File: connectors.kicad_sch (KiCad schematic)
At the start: 4 parts, among them J1 Conn_02x03_Odd_Even, J2 Conn_01x04_Pin, J3 Conn_01x09_Pin, J4 Conn_01x04_Pin

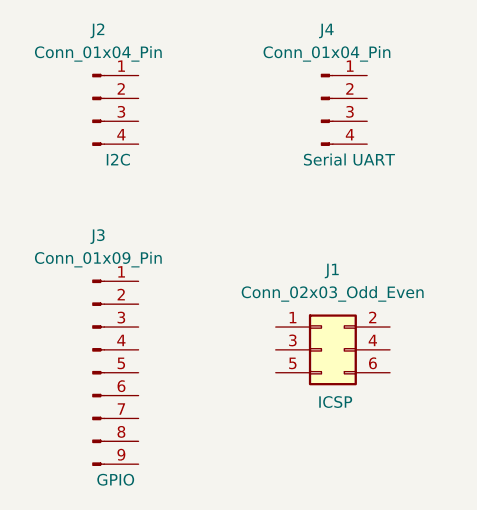
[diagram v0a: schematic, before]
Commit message: completed symbol-footprint association.
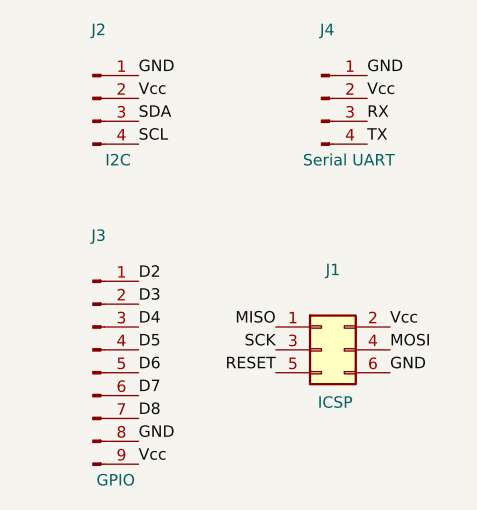
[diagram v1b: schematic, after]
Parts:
- J1: footprint (none) -> Connector_PinHeader_2.54mm:PinHeader_2x03_P2.54mm_Vertical
- J2, J4: footprint (none) -> Connector_PinHeader_2.54mm:PinHeader_1x04_P2.54mm_Vertical
- J3: footprint (none) -> Connector_PinHeader_2.54mm:PinHeader_1x09_P2.54mm_Vertical
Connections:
- net D2: now reaches J3.1 (Pin_1)
- net D3: now reaches J3.2 (Pin_2)
- net D4: now reaches J3.3 (Pin_3)
- net D5: now reaches J3.4 (Pin_4)
- net D6: now reaches J3.5 (Pin_5)
- net D7: now reaches J3.6 (Pin_6)
- net D8: now reaches J3.7 (Pin_7)
- net GND: now reaches J3.8 (Pin_8)
- net GND: now also J1.6 (Pin_6), J2.1 (Pin_1), J4.1 (Pin_1)
- net Vcc: now reaches J3.9 (Pin_9)
- net Vcc: now also J1.2 (Pin_2), J2.2 (Pin_2), J4.2 (Pin_2)
- net SDA: now reaches J2.3 (Pin_3)
- net SCL: now reaches J2.4 (Pin_4)
- net MISO: now reaches J1.1 (Pin_1)
- net SCK: now reaches J1.3 (Pin_3)
- net MOSI: now reaches J1.4 (Pin_4)
- net RESET: now reaches J1.5 (Pin_5)
- net RX: now reaches J4.3 (Pin_3)
- net TX: now reaches J4.4 (Pin_4)
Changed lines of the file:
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@@
 	(generator_version "9.0")
 	(paper "A4")
+	(label "GND"
+		(at 144.78 116.84 0)
+		(effects
+			(font
+				(size 1.27 1.27)
+			)
+			(justify left bottom)
+		)
+	)
+	(label "MISO"
+		(at 132.08 111.76 180)
+		(effects
+			(font
+				(size 1.27 1.27)
+			)
+			(justify right bottom)
+		)
+	)
+	(label "D8"
+		(at 116.84 121.92 0)
+		(effects
+			(font
+				(size 1.27 1.27)
+			)
+			(justify left bottom)
+		)
+	)
+	(label "MOSI"
+		(at 144.78 114.3 0)
+		(effects
+			(font
+				(size 1.27 1.27)
+			)
+			(justify left bottom)
+		)
+	)
+	(label "Vcc"
+		(at 144.78 111.76 0)
+		(effects
+			(font
+				(size 1.27 1.27)
+			)
+			(justify left bottom)
+		)
+	)
+	(label "D5"
+		(at 116.84 114.3 0)
+		(effects
+			(font
+				(size 1.27 1.27)
+			)
+			(justify left bottom)
+		)
+	)
+	(label "SDA"
+		(at 116.84 88.9 0)
+		(effects
+			(font
+				(size 1.27 1.27)
+			)
+			(justify left bottom)
+		)
+	)
+	(label "RX"
+		(at 142.24 88.9 0)
+		(effects
+			(font
+				(size 1.27 1.27)
+			)
+			(justify left bottom)
+		)
+	)
+	(label "TX"
+		(at 142.24 91.44 0)
+		(effects
+			(font
+				(size 1.27 1.27)
+			)
+			(justify left bottom)
+		)
+	)
+	(label "D7"
+		(at 116.84 119.38 0)
+		(effects
+			(font
+				(size 1.27 1.27)
+			)
+			(justify left bottom)
+		)
+	)
+	(label "SCK"
+		(at 132.08 114.3 180)
+		(effects
+			(font
+				(size 1.27 1.27)
+			)
+			(justify right bottom)
+		)
+	)
+	(label "D3"
+		(at 116.84 109.22 0)
+		(effects
+			(font
+				(size 1.27 1.27)
+			)
+			(justify left bottom)
+		)
+	)
+	(label "Vcc"
+		(at 116.84 127 0)
+		(effects
+			(font
+				(size 1.27 1.27)
+			)
+			(justify left bottom)
+		)
+	)
+	(label "GND"
+		(at 116.84 124.46 0)
+		(effects
+			(font
+				(size 1.27 1.27)
+			)
+			(justify left bottom)
+		)
+	)
+	(label "Vcc"
+		(at 116.84 86.36 0)
+		(effects
+			(font
+				(size 1.27 1.27)
+			)
+			(justify left bottom)
+		)
+	)
+	(label "GND"
+		(at 116.84 83.82 0)
+		(effects
+			(font
+				(size 1.27 1.27)
+			)
+			(justify left bottom)
+		)
+	)
+	(label "D2"
+		(at 116.84 106.68 0)
+		(effects
+			(font
+				(size 1.27 1.27)
+			)
+			(justify left bottom)
+		)
+	)
+	(label "GND"
+		(at 142.24 83.82 0)
+		(effects
+			(font
+				(size 1.27 1.27)
+			)
+			(justify left bottom)
+		)
+	)
+	(label "D4"
+		(at 116.84 111.76 0)
+		(effects
+			(font
+				(size 1.27 1.27)
+			)
+			(justify left bottom)
+		)
+	)
+	(label "SCL"
+		(at 116.84 91.44 0)
+		(effects
+			(font
+				(size 1.27 1.27)
+			)
+			(justify left bottom)
+		)
+	)
+	(label "Vcc"
+		(at 142.24 86.36 0)
+		(effects
+			(font
+				(size 1.27 1.27)
+			)
+			(justify left bottom)
+		)
+	)
+	(label "D6"
+		(at 116.84 116.84 0)
+		(effects
+			(font
+				(size 1.27 1.27)
+			)
+			(justify left bottom)
+		)
+	)
+	(label "RESET"
+		(at 132.08 116.84 180)
+		(effects
+			(font
+				(size 1.27 1.27)
+			)
+			(justify right bottom)
+		)
+	)
 	(symbol
 		(lib_id "Connector:Conn_01x09_Pin")
@@
 					(size 1.27 1.27)
 				)
-			)
-		)
-		(property "Footprint" ""
+				(hide yes)
+			)
+		)
+		(property "Footprint" "Connector_PinHeader_2.54mm:PinHeader_1x09_P2.54mm_Vertical"
 			(at 111.76 116.84 0)
 			(effects
@@
 					(size 1.27 1.27)
 				)
-			)
-		)
-		(property "Footprint" ""
+				(hide yes)
+			)
+		)
+		(property "Footprint" "Connector_PinHeader_2.54mm:PinHeader_1x04_P2.54mm_Vertical"
 			(at 111.76 86.36 0)
 			(effects
@@
 					(size 1.27 1.27)
 				)
-			)
-		)
-		(property "Footprint" ""
+				(hide yes)
+			)
+		)
+		(property "Footprint" "Connector_PinHeader_2.54mm:PinHeader_2x03_P2.54mm_Vertical"
 			(at 137.16 114.3 0)
 			(effects
@@
 					(size 1.27 1.27)
 				)
-			)
-		)
-		(property "Footprint" ""
+				(hide yes)
+			)
+		)
+		(property "Footprint" "Connector_PinHeader_2.54mm:PinHeader_1x04_P2.54mm_Vertical"
 			(at 137.16 86.36 0)
 			(effects

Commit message: Completed wiring in the second sheet.
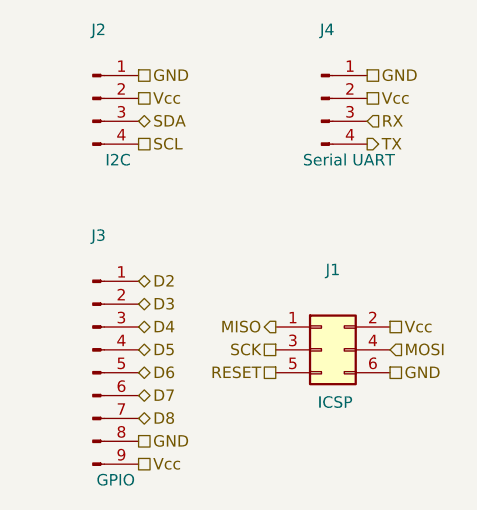
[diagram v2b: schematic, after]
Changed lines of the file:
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@@
 	(generator_version "9.0")
 	(paper "A4")
-	(label "GND"
+	(hierarchical_label "SCK"
+		(shape passive)
+		(at 132.08 114.3 180)
+		(effects
+			(font
+				(size 1.27 1.27)
+			)
+			(justify right)
+		)
+	)
+	(hierarchical_label "TX"
+		(shape output)
+		(at 142.24 91.44 0)
+		(effects
+			(font
+				(size 1.27 1.27)
+			)
+			(justify left)
+		)
+	)
+	(hierarchical_label "D3"
+		(shape bidirectional)
+		(at 116.84 109.22 0)
+		(effects
+			(font
+				(size 1.27 1.27)
+			)
+			(justify left)
+		)
+	)
+	(hierarchical_label "D6"
+		(shape bidirectional)
+		(at 116.84 116.84 0)
+		(effects
+			(font
+				(size 1.27 1.27)
+			)
+			(justify left)
+		)
+	)
+	(hierarchical_label "GND"
+		(shape passive)
+		(at 116.84 83.82 0)
+		(effects
+			(font
+				(size 1.27 1.27)
+			)
+			(justify left)
+		)
+	)
+	(hierarchical_label "D7"
+		(shape bidirectional)
+		(at 116.84 119.38 0)
+		(effects
+			(font
+				(size 1.27 1.27)
+			)
+			(justify left)
+		)
+	)
+	(hierarchical_label "Vcc"
+		(shape passive)
+		(at 116.84 127 0)
+		(effects
+			(font
+				(size 1.27 1.27)
+			)
+			(justify left)
+		)
+	)
+	(hierarchical_label "GND"
+		(shape passive)
+		(at 142.24 83.82 0)
+		(effects
+			(font
+				(size 1.27 1.27)
+			)
+			(justify left)
+		)
+	)
+	(hierarchical_label "RESET"
+		(shape passive)
+		(at 132.08 116.84 180)
+		(effects
+			(font
+				(size 1.27 1.27)
+			)
+			(justify right)
+		)
+	)
+	(hierarchical_label "Vcc"
+		(shape passive)
+		(at 142.24 86.36 0)
+		(effects
+			(font
+				(size 1.27 1.27)
+			)
+			(justify left)
+		)
+	)
+	(hierarchical_label "D2"
+		(shape bidirectional)
+		(at 116.84 106.68 0)
+		(effects
+			(font
+				(size 1.27 1.27)
+			)
+			(justify left)
+		)
+	)
+	(hierarchical_label "D8"
+		(shape bidirectional)
+		(at 116.84 121.92 0)
+		(effects
+			(font
+				(size 1.27 1.27)
+			)
+			(justify left)
+		)
+	)
+	(hierarchical_label "SCL"
+		(shape passive)
+		(at 116.84 91.44 0)
+		(effects
+			(font
+				(size 1.27 1.27)
+			)
+			(justify left)
+		)
+	)
+	(hierarchical_label "RX"
+		(shape input)
+		(at 142.24 88.9 0)
+		(effects
+			(font
+				(size 1.27 1.27)
+			)
+			(justify left)
+		)
+	)
+	(hierarchical_label "Vcc"
+		(shape passive)
+		(at 144.78 111.76 0)
+		(effects
+			(font
+				(size 1.27 1.27)
+			)
+			(justify left)
+		)
+	)
+	(hierarchical_label "MOSI"
+		(shape input)
+		(at 144.78 114.3 0)
+		(effects
+			(font
+				(size 1.27 1.27)
+			)
+			(justify left)
+		)
+	)
+	(hierarchical_label "GND"
+		(shape passive)
 		(at 144.78 116.84 0)
 		(effects
@@
 				(size 1.27 1.27)
 			)
-			(justify left bottom)
-		)
-	)
-	(label "MISO"
+			(justify left)
+		)
+	)
+	(hierarchical_label "D4"
+		(shape bidirectional)
+		(at 116.84 111.76 0)
+		(effects
+			(font
+				(size 1.27 1.27)
+			)
+			(justify left)
+		)
+	)
+	(hierarchical_label "D5"
+		(shape bidirectional)
+		(at 116.84 114.3 0)
+		(effects
+			(font
+				(size 1.27 1.27)
+			)
+			(justify left)
+		)
+	)
+	(hierarchical_label "Vcc"
+		(shape passive)
+		(at 116.84 86.36 0)
+		(effects
+			(font
+				(size 1.27 1.27)
+			)
+			(justify left)
+		)
+	)
+	(hierarchical_label "MISO"
+		(shape output)
 		(at 132.08 111.76 180)
 		(effects
@@
 				(size 1.27 1.27)
 			)
-			(justify right bottom)
-		)
-	)
-	(label "D8"
-		(at 116.84 121.92 0)
-		(effects
-			(font
-				(size 1.27 1.27)
-			)
-			(justify left bottom)
-		)
-	)
-	(label "MOSI"
-		(at 144.78 114.3 0)
-		(effects
-			(font
-				(size 1.27 1.27)
-			)
-			(justify left bottom)
-		)
-	)
-	(label "Vcc"
-		(at 144.78 111.76 0)
-		(effects
-			(font
-				(size 1.27 1.27)
-			)
-			(justify left bottom)
-		)
-	)
-	(label "D5"
-		(at 116.84 114.3 0)
-		(effects
-			(font
-				(size 1.27 1.27)
-			)
-			(justify left bottom)
-		)
-	)
-	(label "SDA"
+			(justify right)
+		)
+	)
+	(hierarchical_label "GND"
+		(shape passive)
+		(at 116.84 124.46 0)
+		(effects
+			(font
+				(size 1.27 1.27)
+			)
+			(justify left)
+		)
+	)
+	(hierarchical_label "SDA"
+		(shape bidirectional)
 		(at 116.84 88.9 0)
 		(effects
@@
 				(size 1.27 1.27)
 			)
-			(justify left bottom)
-		)
-	)
-	(label "RX"
-		(at 142.24 88.9 0)
-		(effects
-			(font
-				(size 1.27 1.27)
-			)
-			(justify left bottom)
-		)
-	)
-	(label "TX"
-		(at 142.24 91.44 0)
-		(effects
-			(font
-				(size 1.27 1.27)
-			)
-			(justify left bottom)
-		)
-	)
-	(label "D7"
-		(at 116.84 119.38 0)
-		(effects
-			(font
-				(size 1.27 1.27)
-			)
-			(justify left bottom)
-		)
-	)
-	(label "SCK"
-		(at 132.08 114.3 180)
-		(effects
-			(font
-				(size 1.27 1.27)
-			)
-			(justify right bottom)
-		)
-	)
-	(label "D3"
-		(at 116.84 109.22 0)
-		(effects
-			(font
-				(size 1.27 1.27)
-			)
-			(justify left bottom)
-		)
-	)
-	(label "Vcc"
-		(at 116.84 127 0)
-		(effects
-			(font
-				(size 1.27 1.27)
-			)
-			(justify left bottom)
-		)
-	)
-	(label "GND"
-		(at 116.84 124.46 0)
-		(effects
-			(font
-				(size 1.27 1.27)
-			)
-			(justify left bottom)
-		)
-	)
-	(label "Vcc"
-		(at 116.84 86.36 0)
-		(effects
-			(font
-				(size 1.27 1.27)
-			)
-			(justify left bottom)
-		)
-	)
-	(label "GND"
-		(at 116.84 83.82 0)
-		(effects
-			(font
-				(size 1.27 1.27)
-			)
-			(justify left bottom)
-		)
-	)
-	(label "D2"
-		(at 116.84 106.68 0)
-		(effects
-			(font
-				(size 1.27 1.27)
-			)
-			(justify left bottom)
-		)
-	)
-	(label "GND"
-		(at 142.24 83.82 0)
-		(effects
-			(font
-				(size 1.27 1.27)
-			)
-			(justify left bottom)
-		)
-	)
-	(label "D4"
-		(at 116.84 111.76 0)
-		(effects
-			(font
-				(size 1.27 1.27)
-			)
-			(justify left bottom)
-		)
-	)
-	(label "SCL"
-		(at 116.84 91.44 0)
-		(effects
-			(font
-				(size 1.27 1.27)
-			)
-			(justify left bottom)
-		)
-	)
-	(label "Vcc"
-		(at 142.24 86.36 0)
-		(effects
-			(font
-				(size 1.27 1.27)
-			)
-			(justify left bottom)
-		)
-	)
-	(label "D6"
-		(at 116.84 116.84 0)
-		(effects
-			(font
-				(size 1.27 1.27)
-			)
-			(justify left bottom)
-		)
-	)
-	(label "RESET"
-		(at 132.08 116.84 180)
-		(effects
-			(font
-				(size 1.27 1.27)
-			)
-			(justify right bottom)
-		)
-	)
+			(justify left)
+		)
+	)
